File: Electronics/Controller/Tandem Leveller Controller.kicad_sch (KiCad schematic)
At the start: 8 parts, among them J1 Conn_01x02, U3 TEENSY 4.0

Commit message: Working on schematic. Added datasheets.
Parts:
- added D7: HSMS-C190, Diode_SMD:D_0603_1608Metric, symbol Device:LED
- added R25: 287, Resistor_SMD:R_0805_2012Metric, symbol Device:R
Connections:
- net +5V: now also D7.2 (A)
- net GND: now also R25.2
- new net: D7.1 (K), R25.1
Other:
- added sheet Valve Control (Valve Control.kicad_sch)
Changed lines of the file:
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@@
   (title_block
     (title "Tandem Leveller Controller")
-    (date "2025-02-13")
+    (date "2025-02-14")
     (rev "V1.0")
     (company "(C) andy@britishideas.com 2025")
@@
     (stroke (width 0) (type default))
   )
+  (wire (pts (xy 201.93 48.26) (xy 201.93 50.165))
+    (stroke (width 0) (type default))
+  )
+  (wire (pts (xy 201.93 29.845) (xy 201.93 31.115))
+    (stroke (width 0) (type default))
+  )
   (wire (pts (xy 261.62 48.26) (xy 261.62 52.07))
     (stroke (width 0) (type default))
   )
   (wire (pts (xy 105.41 95.885) (xy 107.95 95.885))
+    (stroke (width 0) (type default))
+  )
+  (wire (pts (xy 201.93 38.735) (xy 201.93 40.64))
     (stroke (width 0) (type default))
   )
@@
     )
   )
+  (symbol (lib_id "power:+5V") (at 201.93 29.845 0) (unit 1)
+    (in_bom yes) (on_board yes) (dnp no)
+    (property "Reference" "#PWR055" (at 201.93 33.655 0)
+      (effects (font (size 1.27 1.27)) hide)
+    )
+    (property "Value" "+5V" (at 201.93 25.4 0)
+      (effects (font (size 1.27 1.27)))
+    )
+    (property "Footprint" "" (at 201.93 29.845 0)
+      (effects (font (size 1.27 1.27)) hide)
+    )
+    (property "Datasheet" "" (at 201.93 29.845 0)
+      (effects (font (size 1.27 1.27)) hide)
+    )
+    (pin "1")
+    (instances
+      (project "Tandem Leveller Controller"
+        (path "/56ffd1a6-bbed-43b6-8aa8-f23f49f76448"
+          (reference "#PWR055") (unit 1)
+        )
+      )
+    )
+  )
   (symbol (lib_id "power:+5V") (at 242.57 29.845 0) (unit 1)
     (in_bom yes) (on_board yes) (dnp no)
@@
         (path "/56ffd1a6-bbed-43b6-8aa8-f23f49f76448"
           (reference "D6") (unit 1)
+        )
+      )
+    )
+  )
+  (symbol (lib_id "Device:LED") (at 201.93 34.925 90) (unit 1)
+    (in_bom yes) (on_board yes) (dnp no) (fields_autoplaced)
+    (property "Reference" "D7" (at 205.105 35.2424 90)
+      (effects (font (size 1.27 1.27)) (justify right))
+    )
+    (property "Value" "HSMS-C190" (at 205.105 37.7824 90)
+      (effects (font (size 1.27 1.27)) (justify right))
+    )
+    (property "Footprint" "Diode_SMD:D_0603_1608Metric" (at 201.93 34.925 0)
+      (effects (font (size 1.27 1.27)) hide)
+    )
+    (property "Datasheet" "~" (at 201.93 34.925 0)
+      (effects (font (size 1.27 1.27)) hide)
+    )
+    (property "manf#" "HSMS-C190" (at 201.93 34.925 90)
+      (effects (font (size 1.27 1.27)) hide)
+    )
+    (pin "1")
+    (pin "2")
+    (instances
+      (project "Tandem Leveller Controller"
+        (path "/56ffd1a6-bbed-43b6-8aa8-f23f49f76448"
+          (reference "D7") (unit 1)
         )
       )
@@
     )
   )
+  (symbol (lib_id "power:GND") (at 201.93 50.165 0) (unit 1)
+    (in_bom yes) (on_board yes) (dnp no)
+    (property "Reference" "#PWR062" (at 201.93 56.515 0)
+      (effects (font (size 1.27 1.27)) hide)
+    )
+    (property "Value" "GND" (at 201.93 53.975 0)
+      (effects (font (size 1.27 1.27)))
+    )
+    (property "Footprint" "" (at 201.93 50.165 0)
+      (effects (font (size 1.27 1.27)) hide)
+    )
+    (property "Datasheet" "" (at 201.93 50.165 0)
+      (effects (font (size 1.27 1.27)) hide)
+    )
+    (pin "1")
+    (instances
+      (project "Tandem Leveller Controller"
+        (path "/56ffd1a6-bbed-43b6-8aa8-f23f49f76448"
+          (reference "#PWR062") (unit 1)
+        )
+      )
+    )
+  )
   (symbol (lib_id "Device:LED") (at 242.57 34.925 90) (unit 1)
     (in_bom yes) (on_board yes) (dnp no) (fields_autoplaced)
@@
         (path "/56ffd1a6-bbed-43b6-8aa8-f23f49f76448"
           (reference "#PWR049") (unit 1)
+        )
+      )
+    )
+  )
+  (symbol (lib_id "Device:R") (at 201.93 44.45 0) (unit 1)
+    (in_bom yes) (on_board yes) (dnp no) (fields_autoplaced)
+    (property "Reference" "R25" (at 204.47 43.18 0)
+      (effects (font (size 1.27 1.27)) (justify left))
+    )
+    (property "Value" "287" (at 204.47 45.72 0)
+      (effects (font (size 1.27 1.27)) (justify left))
+    )
+    (property "Footprint" "Resistor_SMD:R_0805_2012Metric" (at 200.152 44.45 90)
+      (effects (font (size 1.27 1.27)) hide)
+    )
+    (property "Datasheet" "~" (at 201.93 44.45 0)
+      (effects (font (size 1.27 1.27)) hide)
+    )
+    (pin "1")
+    (pin "2")
+    (instances
+      (project "Tandem Leveller Controller"
+        (path "/56ffd1a6-bbed-43b6-8aa8-f23f49f76448"
+          (reference "R25") (unit 1)
         )
       )
@@
       )
     )
+  )
+  (sheet (at 25.4 132.715) (size 47.625 33.02) (fields_autoplaced)
+    (stroke (width 0.1524) (type solid))
+    (fill (color 0 0 0 0.0000))
+    (property "Sheetname" "Valve Control" (at 25.4 132.0034 0)
+      (effects (font (size 1.27 1.27)) (justify left bottom))
+    )
+    (property "Sheetfile" "Valve Control.kicad_sch" (at 25.4 166.3196 0)
+      (effects (font (size 1.27 1.27)) (justify left top))
+    )
+    (instances
+      (project "Tandem Leveller Controller"
+        (path "/56ffd1a6-bbed-43b6-8aa8-f23f49f76448" (page "8"))
+      )
+    )

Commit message: Working on schematic.
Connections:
- net STATUS3 is gone; now on net STATUS2: R19.2, U3.4 (GPIO2)
- net STATUS1: now also R18.2, U3.3 (GPIO1_CTX2_TX1); no longer R17.2, U3.2 (GPIO0_CRX2_RX1)
- net STATUS2: no longer R18.2, U3.3 (GPIO1_CTX2_TX1)
- net Valve Control/REAR_DIR1: now reaches U3.10 (GPIO8_TX2)
- net Valve Control/REAR_PWM2: now reaches U3.11 (GPIO9)
- net Valve Control/REAR_DIR2: now reaches U3.12 (GPIO10_CS)
- net Switches/~{AUTO_HEIGHT_EN}: now reaches U3.13 (GPIO11_MOSI)
- net Switches/~{SWITCH1}: now reaches U3.14 (GPIO12_MISO)
- net Switches/~{SWITCH2}: now reaches U3.20 (GPIO13_SCK_CRX1)
- net Switches/~{SWITCH3}: now reaches U3.21 (GPIO14_TX3)
- net Valve Control/FRONT_PWM1: now reaches U3.5 (GPIO3)
- net Valve Control/FRONT_DIR1: now reaches U3.6 (GPIO4)
- net Valve Control/FRONT_PWM2: now reaches U3.7 (GPIO5)
- net Valve Control/FRONT_DIR2: now reaches U3.8 (GPIO6)
- net Valve Control/REAR_PWM1: now reaches U3.9 (GPIO7_RX2)
- new net ~{AUTO_HEIGHT_ON}: R17.2, U3.2 (GPIO0_CRX2_RX1)
- no-connect marks 4 -> 9
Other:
- sheet IMU renamed IMU and Sensors
- added sheet Switches (Switches.kicad_sch)
- sheet Valve Control ports: added FRONT_DIR1, FRONT_DIR2, FRONT_PWM1, FRONT_PWM2, REAR_DIR1, REAR_DIR2, REAR_PWM1, REAR_PWM2; removed none
- moved on the sheet: D7, R25

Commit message: Updated schematic. Added footprints for all components.
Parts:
- J1: footprint (none) -> Connector_PinHeader_2.54mm:PinHeader_1x02_P2.54mm_Vertical
- renumbered D7 to D1, D4 to D2, D5 to D3, D6 to D4, R25 to R1, R17 to R2, R18 to R3, R19 to R4, U3 to U1
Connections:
- net Switches/~{MANUAL_REAR_DOWN}: now reaches U1.22 (GPIO15_RX3)
- net Switches/~{SWITCH1} renamed Switches/~{MANUAL_FRONT_UP}
- net Switches/~{SWITCH2} renamed Switches/~{MANUAL_FRONT_DOWN}
- net Switches/~{SWITCH3} renamed Switches/~{MANUAL_REAR_UP}
- no-connect marks 9 -> 8
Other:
- sheet Switches ports: added ~{MANUAL_FRONT_DOWN}, ~{MANUAL_FRONT_UP}, ~{MANUAL_REAR_DOWN}, ~{MANUAL_REAR_UP}; removed ~{SWITCH1}, ~{SWITCH2}, ~{SWITCH3}
- note added: "PWR"

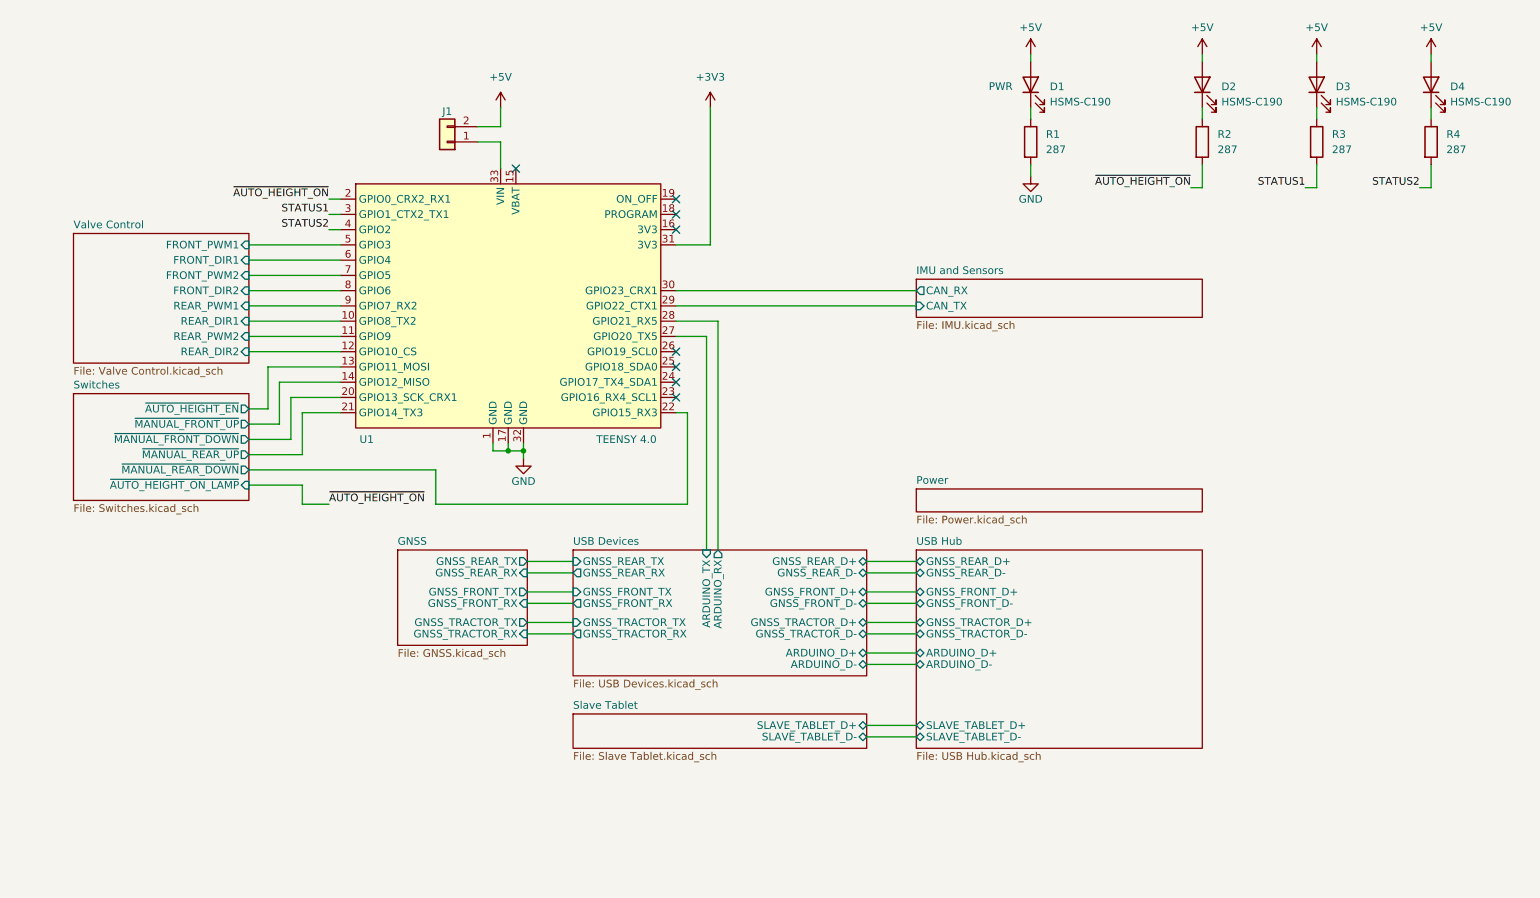
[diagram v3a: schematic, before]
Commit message: Changed switches and lamps. Removed status LEDs. Working on PCB layout.
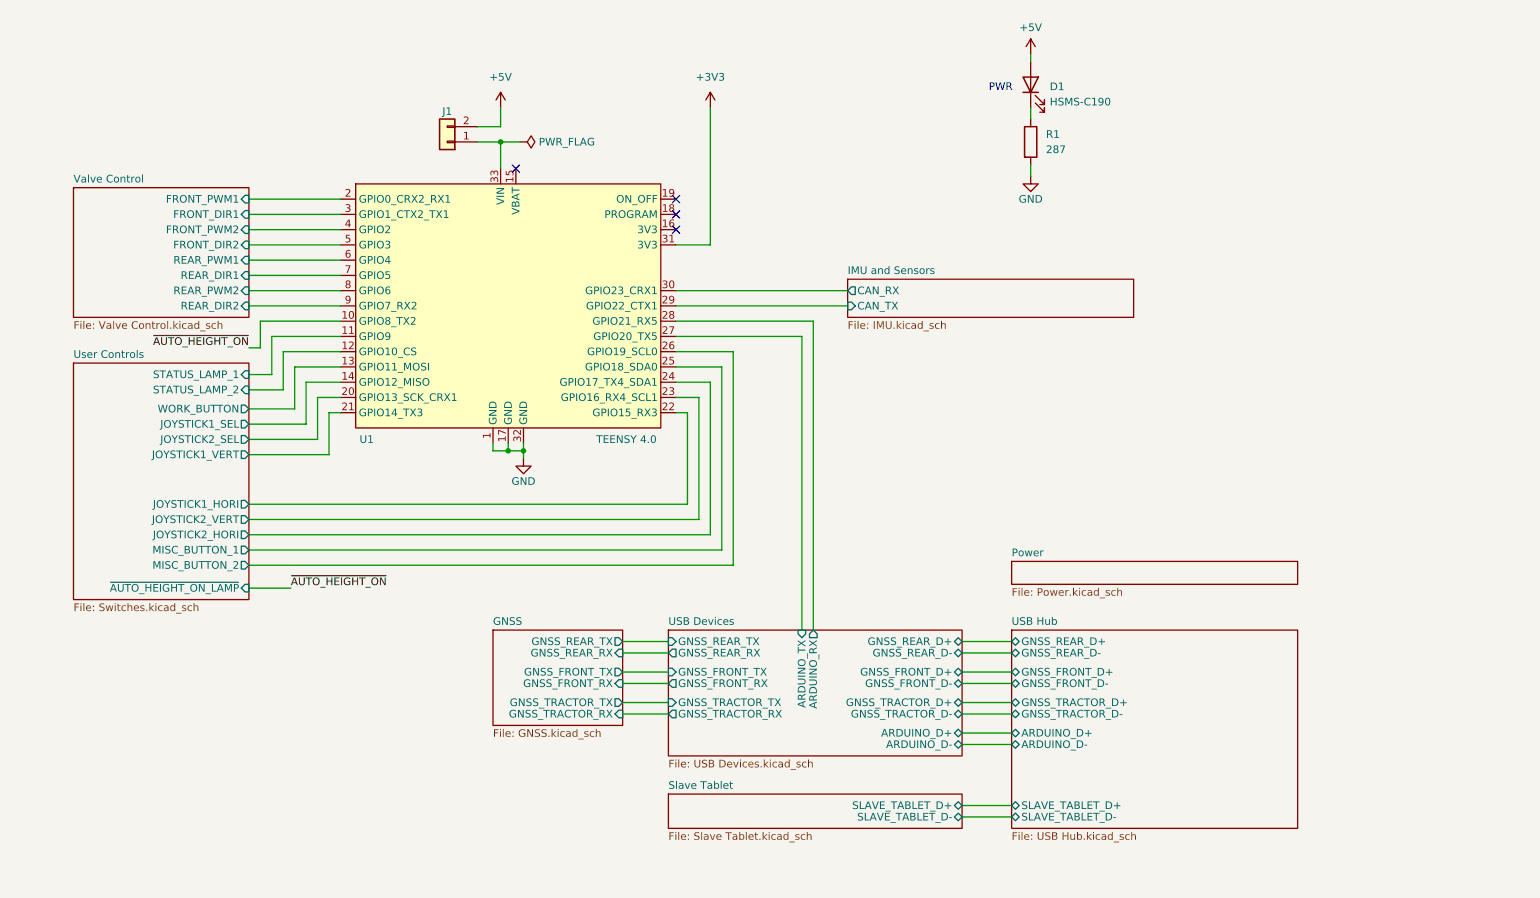
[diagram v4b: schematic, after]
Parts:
- removed D2, D3, D4: HSMS-C190, Diode_SMD:D_0603_1608Metric, symbol Device:LED
- removed R2, R3, R4: 287, Resistor_SMD:R_0805_2012Metric, symbol Device:R
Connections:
- net STATUS1 is gone; now on net Valve Control/FRONT_DIR1: U1.3 (GPIO1_CTX2_TX1)
- net STATUS2 is gone; now on net Valve Control/FRONT_PWM2: U1.4 (GPIO2)
- net Valve Control/FRONT_DIR1: no longer U1.6 (GPIO4)
- net Valve Control/FRONT_DIR2: now also U1.5 (GPIO3); no longer U1.8 (GPIO6)
- net Valve Control/FRONT_PWM1: now also U1.2 (GPIO0_CRX2_RX1); no longer U1.5 (GPIO3)
- net Valve Control/FRONT_PWM2: no longer U1.7 (GPIO5)
- net Valve Control/REAR_DIR1: now also U1.7 (GPIO5); no longer U1.10 (GPIO8_TX2)
- net Valve Control/REAR_DIR2: now also U1.9 (GPIO7_RX2); no longer U1.12 (GPIO10_CS)
- net Valve Control/REAR_PWM1: now also U1.6 (GPIO4); no longer U1.9 (GPIO7_RX2)
- net Valve Control/REAR_PWM2: now also U1.8 (GPIO6); no longer U1.11 (GPIO9)
- net ~{AUTO_HEIGHT_ON}: now also U1.10 (GPIO8_TX2); no longer U1.2 (GPIO0_CRX2_RX1)
- net User Controls/JOYSTICK2_VERT: now reaches U1.23 (GPIO16_RX4_SCL1)
- net User Controls/JOYSTICK2_HORI: now reaches U1.24 (GPIO17_TX4_SDA1)
- net User Controls/MISC_BUTTON_1: now reaches U1.25 (GPIO18_SDA0)
- net User Controls/MISC_BUTTON_2: now reaches U1.26 (GPIO19_SCL0)
- net User Controls/~{AUTO_HEIGHT_EN} renamed User Controls/WORK_BUTTON
- net User Controls/~{MANUAL_FRONT_DOWN} renamed User Controls/JOYSTICK2_SEL
- net User Controls/~{MANUAL_FRONT_UP} renamed User Controls/JOYSTICK1_SEL
- net User Controls/~{MANUAL_REAR_DOWN} renamed User Controls/JOYSTICK1_HORI
- net User Controls/~{MANUAL_REAR_UP} renamed User Controls/JOYSTICK1_VERT
- new net User Controls/STATUS_LAMP_1: U1.11 (GPIO9)
- new net User Controls/STATUS_LAMP_2: U1.12 (GPIO10_CS)
- no-connect marks 8 -> 4
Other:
- sheet Switches renamed User Controls
- sheet User Controls ports: added JOYSTICK1_HORI, JOYSTICK1_SEL, JOYSTICK1_VERT, JOYSTICK2_HORI, JOYSTICK2_SEL, JOYSTICK2_VERT, MISC_BUTTON_1, MISC_BUTTON_2, STATUS_LAMP_1, STATUS_LAMP_2, WORK_BUTTON; removed ~{AUTO_HEIGHT_EN}, ~{MANUAL_FRONT_DOWN}, ~{MANUAL_FRONT_UP}, ~{MANUAL_REAR_DOWN}, ~{MANUAL_REAR_UP}

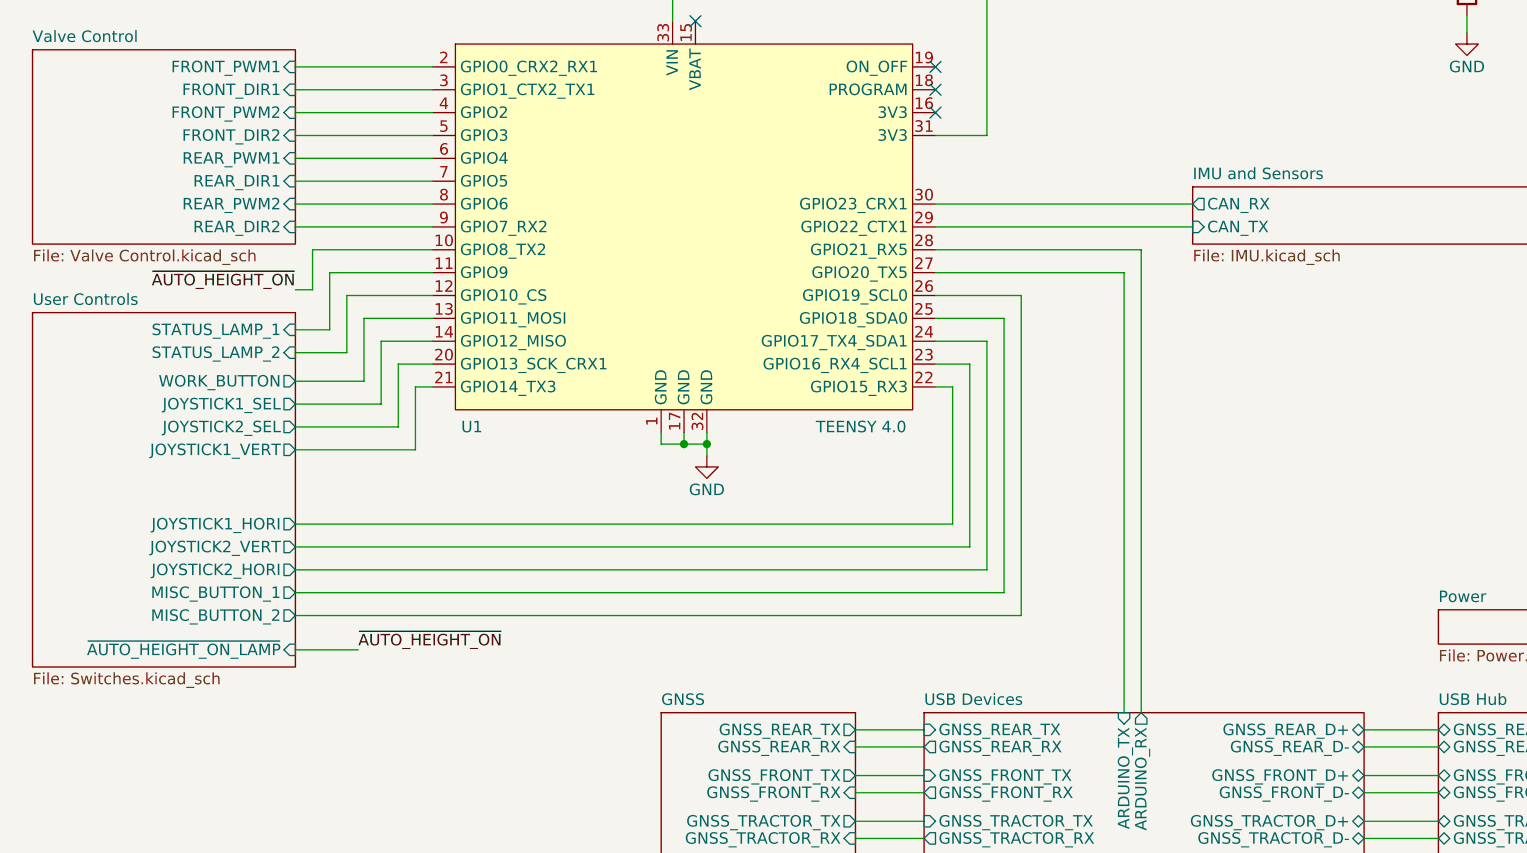
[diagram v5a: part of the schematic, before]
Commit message: Moved controls from GPIO to CAN bus. Added two more CAN bus connectors. Changed GNSS SIM connector from pin header to JST-PH.
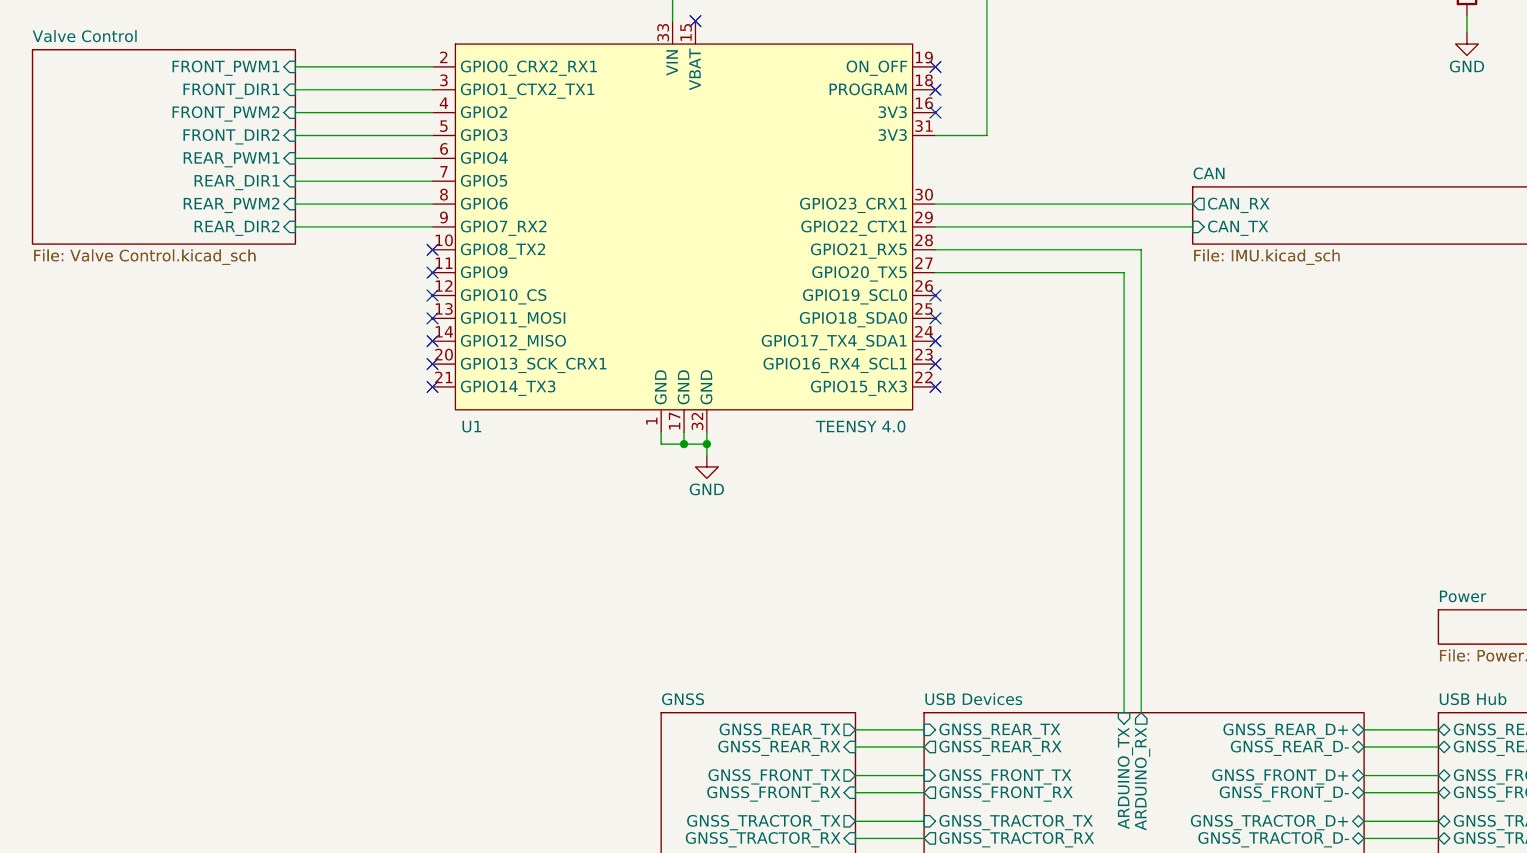
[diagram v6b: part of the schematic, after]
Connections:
- net User Controls/JOYSTICK1_HORI: no longer names the net of U1.22 (GPIO15_RX3)
- net User Controls/JOYSTICK1_SEL: no longer names the net of U1.14 (GPIO12_MISO)
- net User Controls/JOYSTICK1_VERT: no longer names the net of U1.21 (GPIO14_TX3)
- net User Controls/JOYSTICK2_HORI: no longer names the net of U1.24 (GPIO17_TX4_SDA1)
- net User Controls/JOYSTICK2_SEL: no longer names the net of U1.20 (GPIO13_SCK_CRX1)
- net User Controls/JOYSTICK2_VERT: no longer names the net of U1.23 (GPIO16_RX4_SCL1)
- net User Controls/MISC_BUTTON_1: no longer names the net of U1.25 (GPIO18_SDA0)
- net User Controls/MISC_BUTTON_2: no longer names the net of U1.26 (GPIO19_SCL0)
- net User Controls/STATUS_LAMP_1: no longer names the net of U1.11 (GPIO9)
- net User Controls/STATUS_LAMP_2: no longer names the net of U1.12 (GPIO10_CS)
- net User Controls/WORK_BUTTON: no longer names the net of U1.13 (GPIO11_MOSI)
- net ~{AUTO_HEIGHT_ON}: no longer names the net of U1.10 (GPIO8_TX2)
- no-connect marks 4 -> 16
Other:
- sheet IMU and Sensors renamed CAN
- removed sheet User Controls

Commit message: Renamed valve control connectors and reordered pins to match pinout of MDD10A connectors.
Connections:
- net Valve Control/FRONT_DIR1 renamed Valve Control/FRONT_HEIGHT_PWM
- net Valve Control/FRONT_DIR2 renamed Valve Control/REAR_HEIGHT_PWM
- net Valve Control/FRONT_PWM1 renamed Valve Control/FRONT_HEIGHT_DIR
- net Valve Control/FRONT_PWM2 renamed Valve Control/REAR_HEIGHT_DIR
- net Valve Control/REAR_DIR1 renamed Valve Control/FRONT_DUMP_PWM
- net Valve Control/REAR_DIR2 renamed Valve Control/REAR_DUMP_PWM
- net Valve Control/REAR_PWM1 renamed Valve Control/FRONT_DUMP_DIR
- net Valve Control/REAR_PWM2 renamed Valve Control/REAR_DUMP_DIR
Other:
- sheet Valve Control ports: added FRONT_DUMP_DIR, FRONT_DUMP_PWM, FRONT_HEIGHT_DIR, FRONT_HEIGHT_PWM, REAR_DUMP_DIR, REAR_DUMP_PWM, REAR_HEIGHT_DIR, REAR_HEIGHT_PWM; removed FRONT_DIR1, FRONT_DIR2, FRONT_PWM1, FRONT_PWM2, REAR_DIR1, REAR_DIR2, REAR_PWM1, REAR_PWM2
- moved on the sheet: D1, J1, R1, U1
